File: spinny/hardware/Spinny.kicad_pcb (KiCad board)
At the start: 2 copper layers, 60 x 60 mm, 36 parts, among them J1 USB_C_Receptacle_USB2.0, J2 Conn_01x04, SW1 SW_Push, SW2 SW_Push, SW3 SW_Push, SW4 SW_Push, SW5 SW_RST, U1 XC6206P332MR, U2 SRV05-4, U3 STM32F103C8T6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

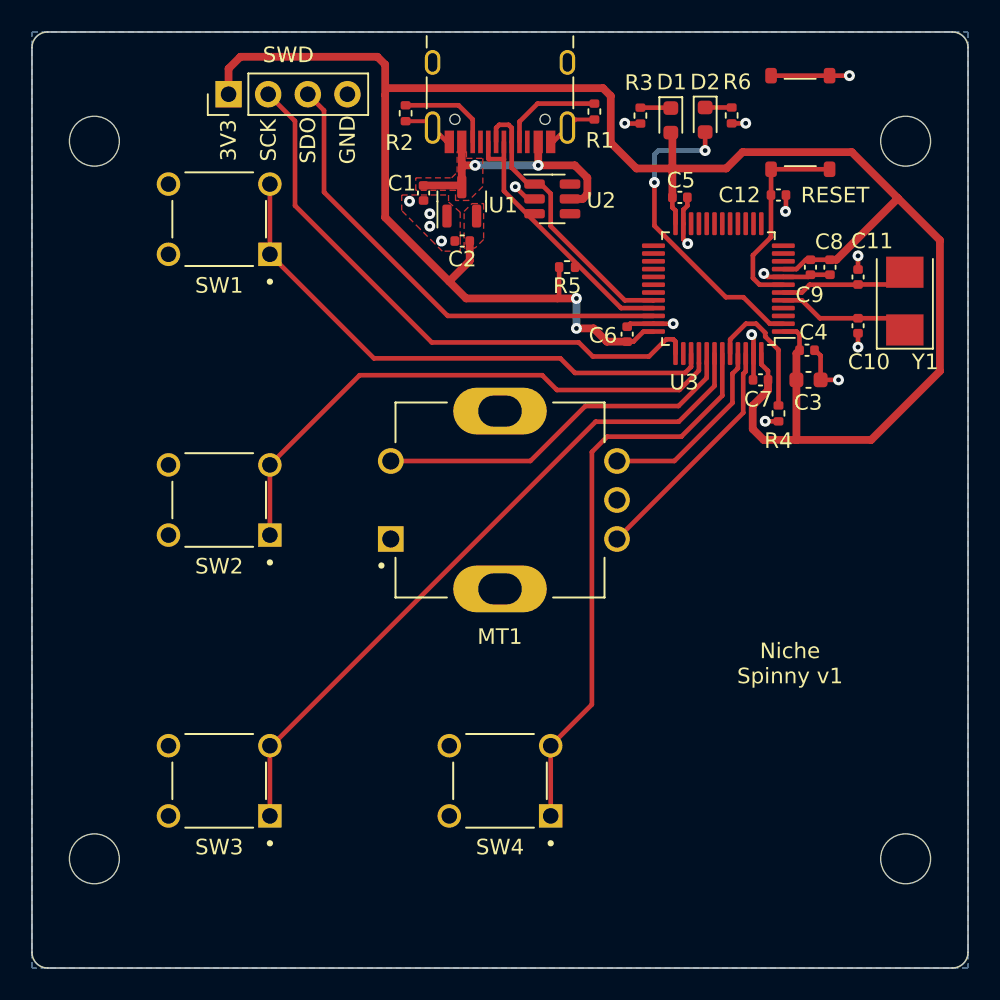
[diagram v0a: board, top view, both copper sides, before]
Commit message: Adjust board to fit enclosure beter
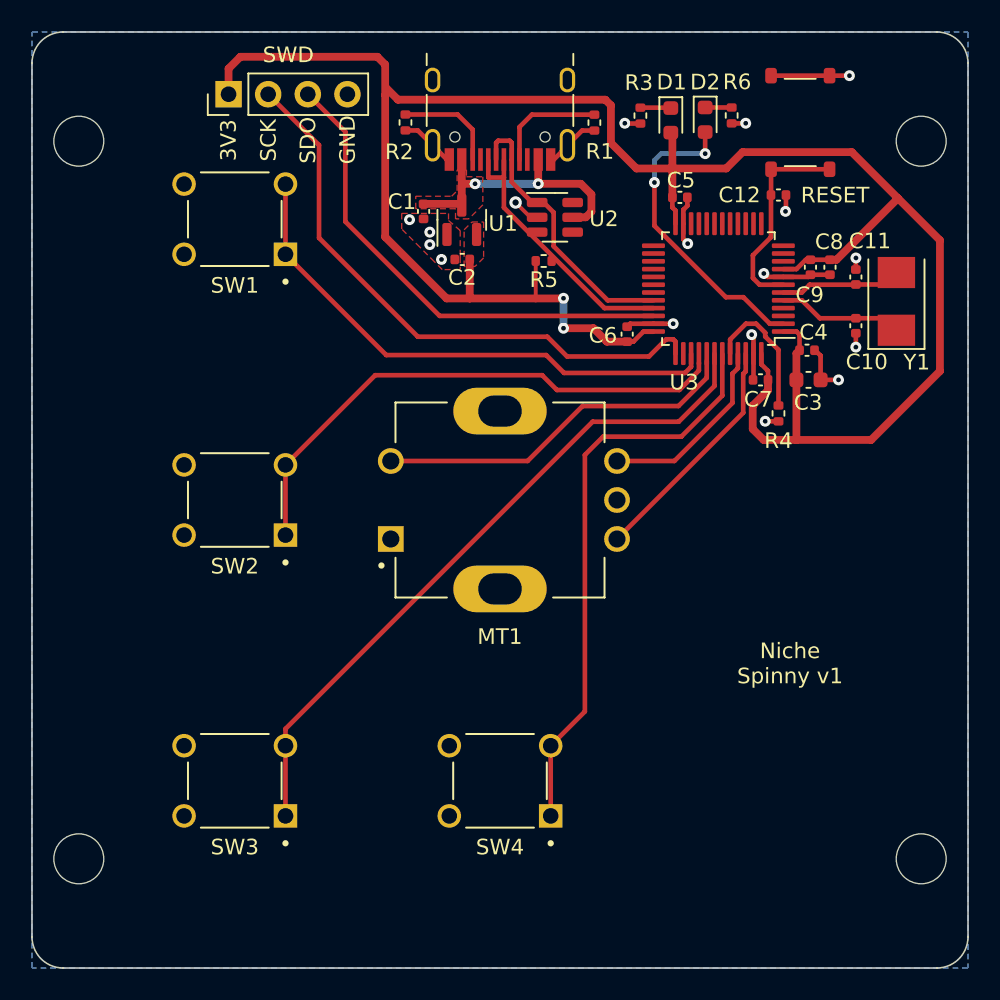
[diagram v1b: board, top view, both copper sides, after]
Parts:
- moved R5 1.55 mm to (152.8, 84.7)
- moved U2 1.19 mm to (153.5, 81.9)
- moved C1 1.18 mm to (145.1, 81.5)
- moved U1 1.18 mm to (147.6, 82.0)
- moved C2 1.18 mm to (147.6, 84.6)
- moved J1 1.13 mm to (150.0, 74.1)
- moved H1 1.00 mm to (123.0, 77.0)
- moved H2 1.00 mm to (177.0, 77.0)
- moved H3 1.00 mm to (123.0, 123.0)
- moved H4 1.00 mm to (177.0, 123.0)
- moved SW1 1.00 mm to (133.0, 82.0)
- moved SW2 1.00 mm to (133.0, 100.0)
- moved SW3 1.00 mm to (133.0, 118.0)
- moved R1 0.71 mm to (156.1, 75.8)
- moved R2 0.59 mm to (143.9, 75.8)
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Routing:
- net BTN_1: track 35.7 -> 34.7 mm
- net BTN_2: track 35.8 -> 34.8 mm
- net Net-(J1-PadA5): track 6.58 -> 7.26 mm
- net USB_D+: track 17.9 -> 17.4 mm
- net +5V: track 17.5 -> 18.1 mm
- net Net-(J1-PadB5): track 6.12 -> 6.63 mm
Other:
- outline, holes or cut-outs redrawn
